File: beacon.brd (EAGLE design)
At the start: 40 x 25.3 mm, 49 parts, among them J1 5-5530843-0MALE, Q1 MMBT3904, Q2 DMG2302UK, U1 AOZ6662DI, U3 ATTINY85, U4 MS5637-02BA03, U5 SI4012, U6 MAAL-010704, U7 MIC5504

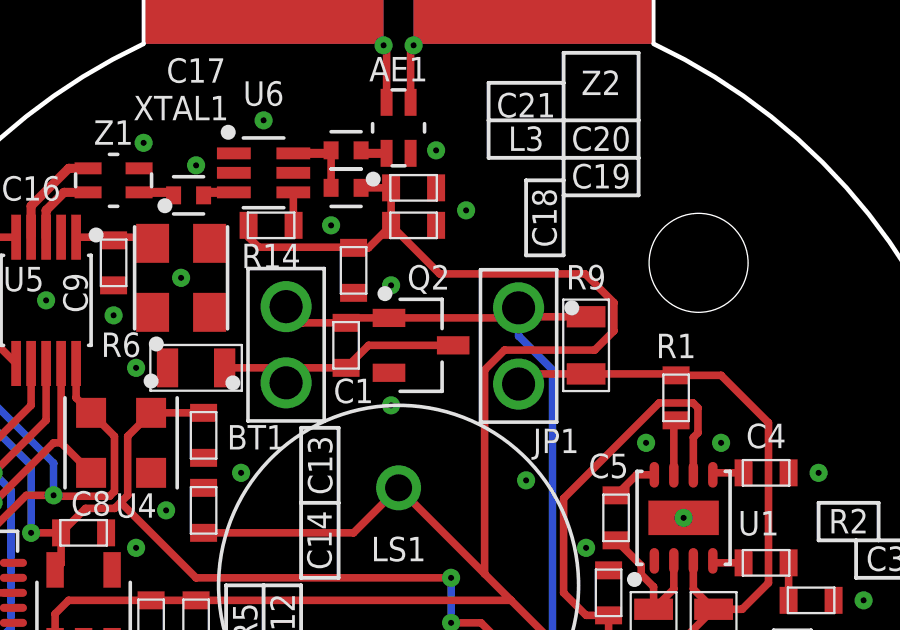
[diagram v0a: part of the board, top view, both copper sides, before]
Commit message: Added PTC fuse
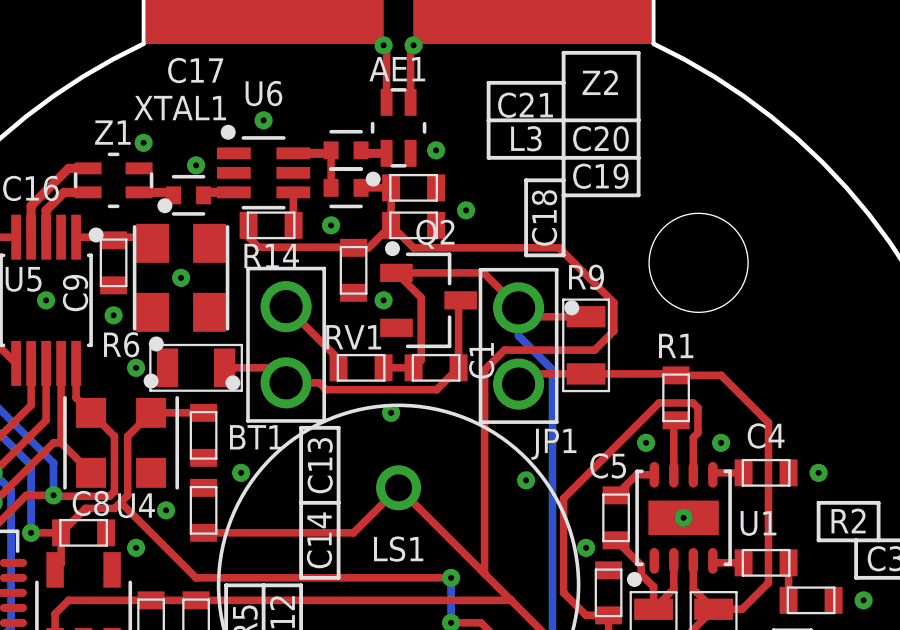
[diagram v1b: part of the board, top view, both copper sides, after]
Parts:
- added RV1: 80mA, radio-tracker:0603
- moved C1 3.09 mm to (21.2, 22.5), turned to 180 degrees
- moved Q2 1.52 mm to (21.0, 24.8)
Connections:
- new net N$12: BT1.2, RV1.P$1
- net VBAT: now also RV1.P$2; no longer BT1.2
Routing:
- net N$12: track 0.00 -> 2.76 mm
- net N$8: track 8.34 -> 10.7 mm
- net VBAT: track 62.0 -> 63.0 mm
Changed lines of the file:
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@@
 <setting verticaltext="up"/>
 </settings>
-<grid distance="9.84251969" unitdist="mil" unit="mil" style="lines" multiple="1" display="no" altdistance="5" altunitdist="mil" altunit="mil"/>
+<grid distance="0.25" unitdist="mm" unit="mm" style="lines" multiple="1" display="no" altdistance="5" altunitdist="mil" altunit="mil"/>
 <layers>
 <layer number="1" name="Top" color="4" fill="1" visible="yes" active="yes"/>
@@
 <attribute name="NAME" x="15.25" y="20.591" size="0.8128" layer="25" rot="R180" align="bottom-center"/>
 </element>
-<element name="C1" library="radio-tracker" package="0603" value="1uF" x="18.25" y="23.25" smashed="yes" rot="R90">
-<attribute name="NAME" x="18.5" y="22.1364" size="0.8128" layer="25" rot="R180" align="bottom-center"/>
+<element name="C1" library="radio-tracker" package="0603" value="1uF" x="21.25" y="22.5" smashed="yes" rot="R180">
+<attribute name="NAME" x="22.3636" y="22.75" size="0.8128" layer="25" rot="R270" align="bottom-center"/>
 </element>
 <element name="C12" library="radio-tracker" package="0603" value="0.1uF" x="3.25" y="18" smashed="yes">
@@
 <attribute name="NAME" x="12.75" y="9.0964" size="0.8128" layer="25" rot="R180" align="bottom-center"/>
 </element>
-<element name="Q2" library="radio-tracker" package="DMG2302UK" package3d_urn="urn:adsk.eagle:package:20410695/1" value="DMG2302UK" x="20.75" y="23.25" smashed="yes">
-<attribute name="NAME" x="21" y="25.1086" size="0.8128" layer="25" align="bottom-center"/>
+<element name="Q2" library="radio-tracker" package="DMG2302UK" package3d_urn="urn:adsk.eagle:package:20410695/1" value="DMG2302UK" x="21" y="24.75" smashed="yes">
+<attribute name="NAME" x="21.25" y="26.6086" size="0.8128" layer="25" align="bottom-center"/>
 </element>
 <element name="R1" library="radio-tracker" package="0603" value="10k" x="29.25" y="21.5" smashed="yes" rot="R90">
@@
 <element name="C9" library="radio-tracker" package="0603" value="10pF" x="10.5" y="26" smashed="yes" rot="R90">
 <attribute name="NAME" x="9.6364" y="25" size="0.8128" layer="25" rot="R90" align="bottom-center"/>
+</element>
+<element name="RV1" library="radio-tracker" package="0603" value="80mA" x="18.75" y="22.5" smashed="yes">
+<attribute name="NAME" x="18.5" y="23.1136" size="0.8128" layer="25" align="bottom-center"/>
 </element>
 </elements>
@@
 <via x="13.25" y="29.25" extent="1-16" drill="0.2"/>
 <via x="21.25" y="29.75" extent="1-16" drill="0.2"/>
-<via x="19.75" y="21.25" extent="1-16" drill="0.2"/>
-<via x="19.75" y="25.25" extent="1-16" drill="0.2"/>
+<via x="19.75" y="21" extent="1-16" drill="0.2"/>
+<via x="19.5" y="24.75" extent="1-16" drill="0.2"/>
 <via x="29.5" y="17.5" extent="1-16" drill="0.2"/>
 <via x="34" y="19" extent="1-16" drill="0.2"/>
@@
 <wire x1="23.531125" y1="23.09195" x2="26.53788125" y2="23.09195" width="0.254" layer="1"/>
 <wire x1="26.53788125" y1="23.09195" x2="27.1771" y2="23.73116875" width="0.254" layer="1"/>
-<wire x1="27.1771" y1="24.67383125" x2="26.21898125" y2="25.63195" width="0.254" layer="1"/>
-<wire x1="21.36805" y1="25.63195" x2="19.75" y2="27.25" width="0.254" layer="1"/>
-<wire x1="27.1771" y1="23.73116875" x2="27.1771" y2="24.67383125" width="0.254" layer="1"/>
-<wire x1="26.21898125" y1="25.63195" x2="21.36805" y2="25.63195" width="0.254" layer="1"/>
+<wire x1="19.75" y1="27.25" x2="20.5" y2="26.5" width="0.254" layer="1"/>
+<wire x1="27.1771" y1="24.67383125" x2="27.1771" y2="23.73116875" width="0.254" layer="1"/>
 <wire x1="22.86805" y1="22.428875" x2="22.86805" y2="15.63195" width="0.254" layer="1"/>
 <wire x1="13.25" y1="14.75" x2="23.75" y2="14.75" width="0.254" layer="1"/>
@@
 <wire x1="27.5" y1="8" x2="28.5475" y2="9.0475" width="0.254" layer="1"/>
 <wire x1="11.75" y1="14.75" x2="13.25" y2="14.75" width="0.254" layer="1"/>
+<wire x1="20.5" y1="26.5" x2="25.35093125" y2="26.5" width="0.254" layer="1"/>
+<wire x1="25.35093125" y1="26.5" x2="27.1771" y2="24.67383125" width="0.254" layer="1"/>
 </signal>
 <signal name="VBAT">
 <contactref element="C1" pad="P$2"/>
-<contactref element="BT1" pad="2"/>
 <contactref element="R9" pad="P$1"/>
 <contactref element="JP1" pad="1"/>
 <contactref element="Q2" pad="1"/>
-<wire x1="16.25" y1="24.54" x2="16.79" y2="24" width="0.254" layer="1"/>
-<wire x1="16.79" y1="24" x2="18.25" y2="24" width="0.254" layer="1"/>
-<wire x1="18.25" y1="24" x2="18.415" y2="24.165" width="0.254" layer="1"/>
-<wire x1="18.415" y1="24.165" x2="19.6796" y2="24.165" width="0.254" layer="1"/>
-<wire x1="19.6796" y1="24.165" x2="23.665" y2="24.165" width="0.254" layer="1"/>
-<wire x1="23.665" y1="24.165" x2="24" y2="24.5" width="0.254" layer="1"/>
 <wire x1="24" y1="24.5" x2="24.2975" y2="24.2025" width="0.254" layer="1"/>
 <wire x1="24.2975" y1="24.2025" x2="26.25" y2="24.2025" width="0.254" layer="1"/>
@@
 <wire x1="25.13195" y1="10.9135375" x2="24.8330125" y2="10.6146" width="0.254" layer="16"/>
 <wire x1="25.13195" y1="22.428875" x2="25.13195" y2="10.9135375" width="0.254" layer="16"/>
+<contactref element="RV1" pad="P$2"/>
+<wire x1="19.5" y1="22.5" x2="20.5" y2="22.5" width="0.254" layer="1"/>
+<wire x1="20.5" y1="22.5" x2="20.7532" y2="22.7532" width="0.254" layer="1"/>
+<wire x1="20.7532" y1="24.8414" x2="19.9296" y2="25.665" width="0.254" layer="1"/>
+<wire x1="20.7532" y1="22.7532" x2="20.7532" y2="24.8414" width="0.254" layer="1"/>
+<wire x1="19.9296" y1="25.665" x2="22.835" y2="25.665" width="0.254" layer="1"/>
+<wire x1="22.835" y1="25.665" x2="24" y2="24.5" width="0.254" layer="1"/>
 </signal>
 <signal name="N$9">
@@
 <wire x1="14.2025" y1="22.5" x2="15.75" y2="22.5" width="0.254" layer="1"/>
 <wire x1="15.75" y1="22.5" x2="16.25" y2="22" width="0.254" layer="1"/>
-<wire x1="16.25" y1="22" x2="16.75" y2="22.5" width="0.254" layer="1"/>
-<wire x1="16.75" y1="22.5" x2="18.25" y2="22.5" width="0.254" layer="1"/>
-<wire x1="18.25" y1="22.5" x2="19" y2="23.25" width="0.254" layer="1"/>
-<wire x1="19" y1="23.25" x2="21.8204" y2="23.25" width="0.254" layer="1"/>
+<wire x1="22" y1="22.5" x2="22" y2="24.6796" width="0.254" layer="1"/>
+<wire x1="22" y1="24.6796" x2="22.0704" y2="24.75" width="0.254" layer="1"/>
+<wire x1="16.25" y1="22" x2="17.35486875" y2="22" width="0.254" layer="1"/>
+<wire x1="17.35486875" y1="22" x2="17.58426875" y2="21.7706" width="0.254" layer="1"/>
+<wire x1="21.2706" y1="21.7706" x2="22" y2="22.5" width="0.254" layer="1"/>
+<wire x1="17.58426875" y1="21.7706" x2="21.2706" y2="21.7706" width="0.254" layer="1"/>
 </signal>
 <signal name="SDN">
@@
 <wire x1="8.25" y1="27.75" x2="8.85" y2="28.35" width="0.3048" layer="1"/>
 </signal>
+<signal name="N$12">
+<contactref element="BT1" pad="2"/>
+<contactref element="RV1" pad="P$1"/>
+<wire x1="16.25" y1="24.54" x2="18" y2="22.79" width="0.254" layer="1"/>
+<wire x1="18" y1="22.79" x2="18" y2="22.5" width="0.254" layer="1"/>
+</signal>
 </signals>

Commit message: Layed out tracker board
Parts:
- added R7: 10k, radio-tracker:0603
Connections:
- net !RESET: now also R7.P$1
- net +3V3: now also R7.P$2
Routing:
- net +3V3: track 70.0 -> 76.6 mm
- net !RESET: track 41.9 -> 42.7 mm
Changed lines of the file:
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@@
 <attribute name="NAME" x="18.5" y="23.1136" size="0.8128" layer="25" align="bottom-center"/>
+</element>
+<element name="R7" library="radio-tracker" package="0603" value="10k" x="2.75" y="12.25" smashed="yes" rot="R180">
+<attribute name="NAME" x="2.75" y="11.3864" size="0.8128" layer="25" rot="R180" align="bottom-center"/>
 </element>
 </elements>
@@
 <wire x1="22.75" y1="14" x2="26.25" y2="10.5" width="0.254" layer="1"/>
 <wire x1="21.75" y1="15.5" x2="21.75" y2="14" width="0.254" layer="16"/>
+<contactref element="R7" pad="P$2"/>
+<wire x1="2" y1="12.25" x2="2" y2="16" width="0.254" layer="1"/>
+<wire x1="2" y1="16" x2="4" y2="18" width="0.254" layer="1"/>
 </signal>
 <signal name="N$8">
@@
 <wire x1="11.25" y1="8.0936" x2="11.25" y2="8" width="0.254" layer="1"/>
 <wire x1="6.5078625" y1="11.4174" x2="8.3316625" y2="9.5936" width="0.254" layer="1"/>
+<contactref element="R7" pad="P$1"/>
+<wire x1="3.5" y1="12.25" x2="4.176075" y2="12.25" width="0.254" layer="1"/>
+<wire x1="4.176075" y1="12.25" x2="4.25" y2="12.176075" width="0.254" layer="1"/>
 </signal>
 <signal name="OC1B">
